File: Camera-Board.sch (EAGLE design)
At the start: 87 parts, among them J1 RJ45KEYSTONE-942, J10 BNC, J11 BNC, J12 BNC, J13 BNC, J14 BNC, J2 JTAG_ARM_10PIN, J3 APP_2POS_CONFIG12V_HORIZ, J4 BNC, J5 BNC, J6 BNC, J7 BNC, J9 BNC, U1 TM4C1294NCPDT, U2 HX1198FNL, U3 SLVU2.8-4, U4 OKI-78SR-5/1.5-W36HC, U5 TPS73733DCQ, U6 MAX4312ESE, U8 MAX4312ESE, Y1 NX3225GA, Y2 CRYATL_32K_SMD

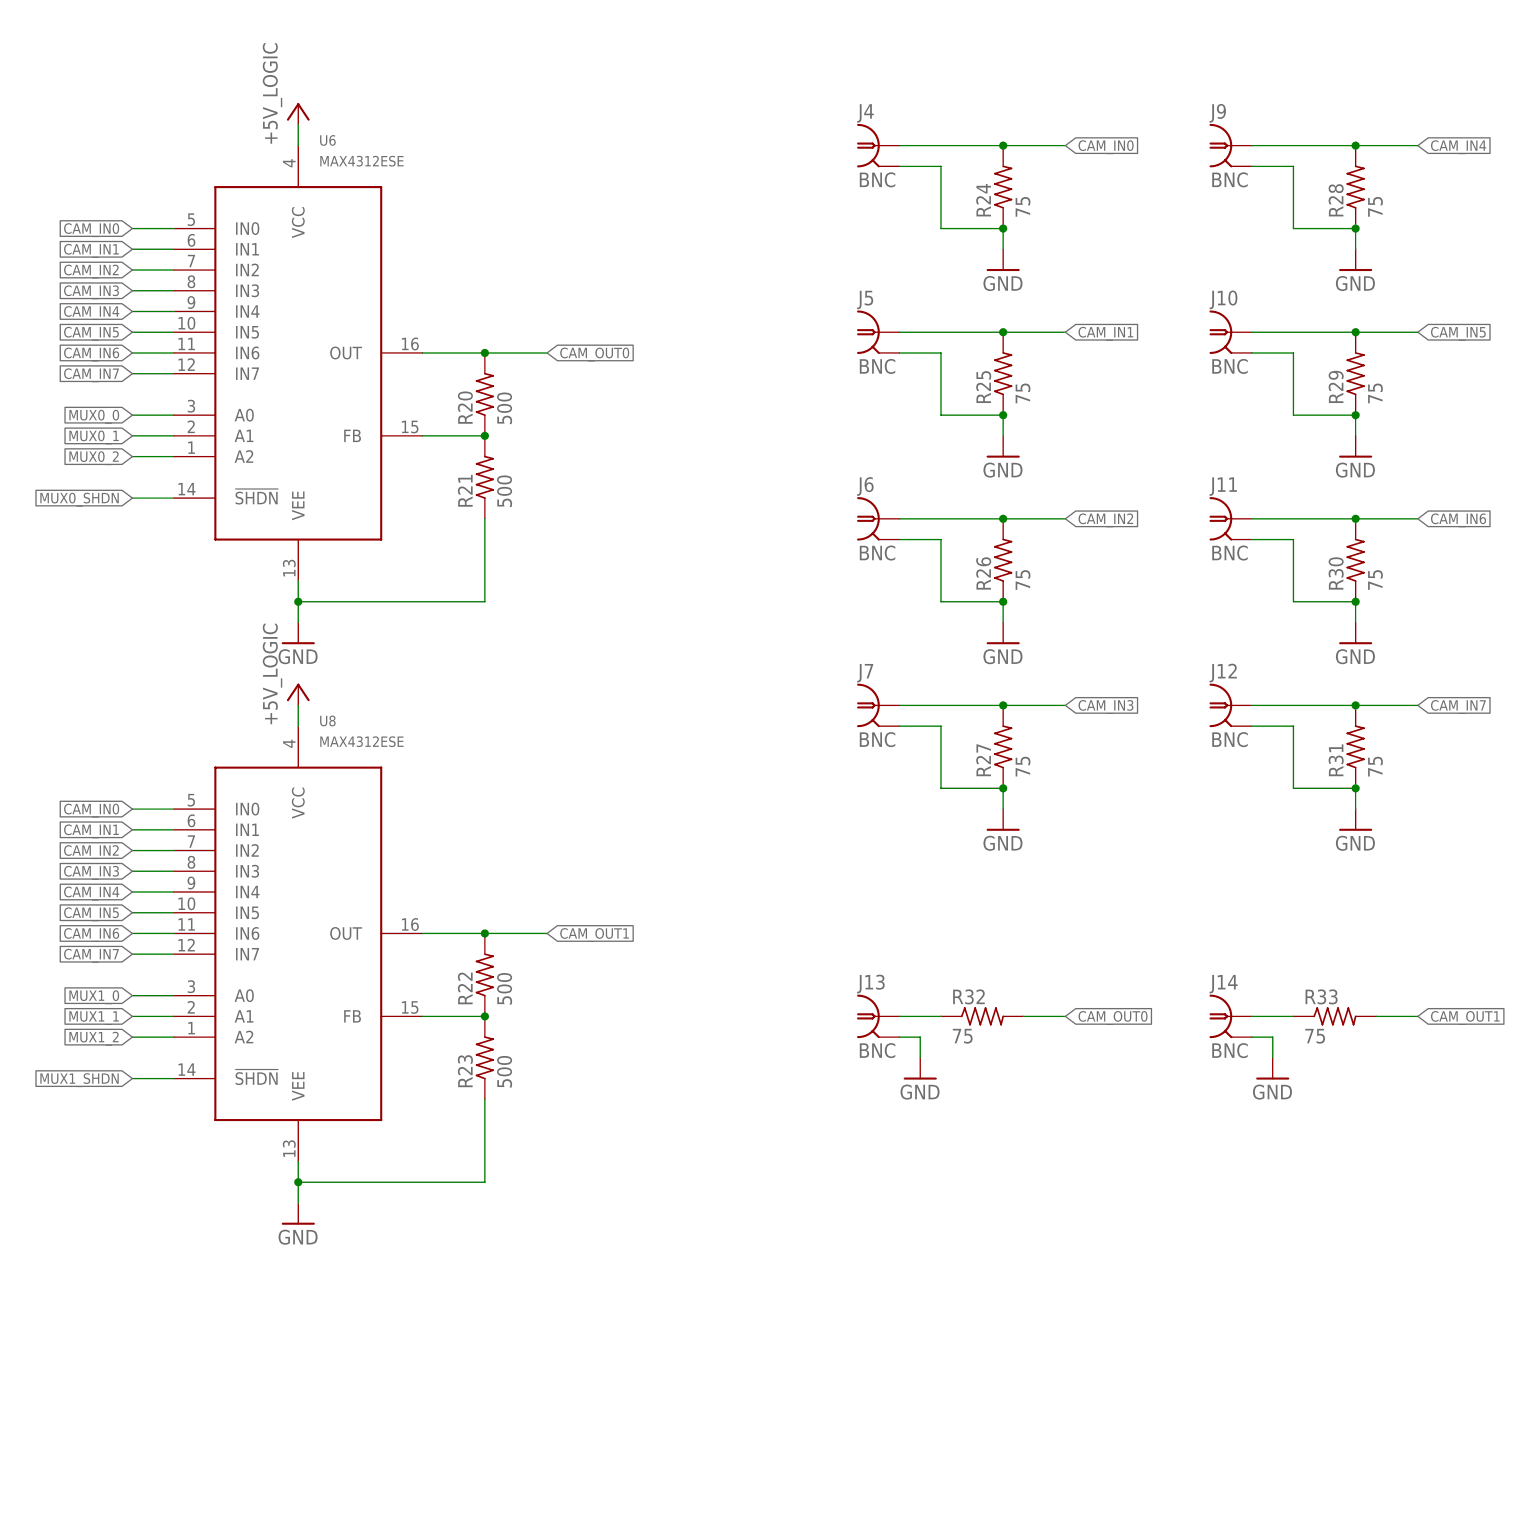
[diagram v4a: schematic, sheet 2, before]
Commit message: Final touches
Made board larger
Added more space between BNCs
Added more mounting holes
Updated Slik text and added signature
Arranged component labels
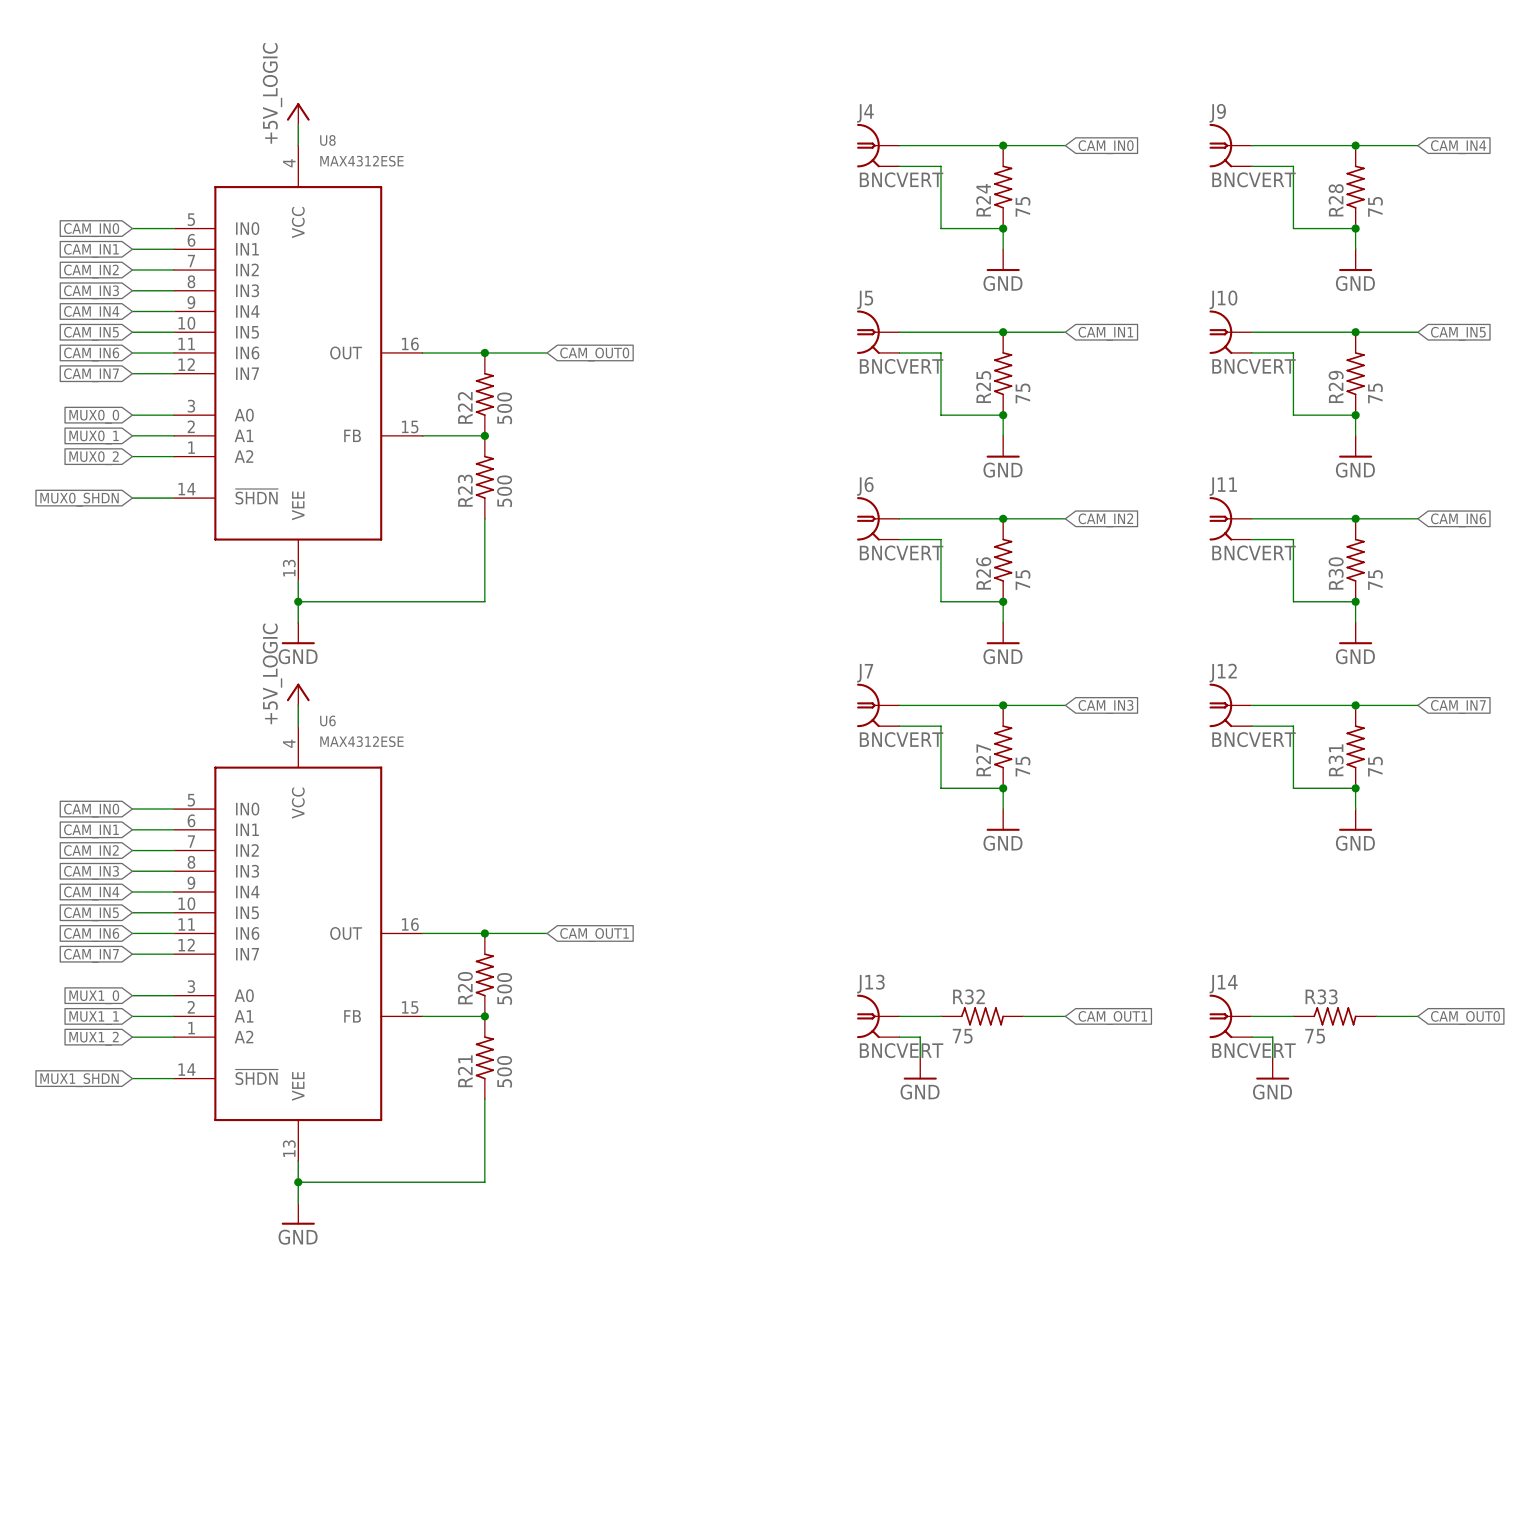
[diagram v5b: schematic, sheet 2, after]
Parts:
- added U$8: SIG3, sig:SIG3
- J10, J11, J12, J13, J14, J4, J5, J6, J7, J9: value BNC -> BNCVERT; device MRDT-Connectors:BNC -> MRDT-Connectors:BNCVERT
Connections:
- net CAM_OUT0: now also R22.2, R33.2, U8.OUT; no longer R20.2, R32.2, U6.OUT
- net CAM_OUT1: now also R20.2, R32.2, U6.OUT; no longer R22.2, R33.2, U8.OUT
- net MUX0_0: now also U1G$1.PD0@1, U8.A0; no longer U1G$1.PD7@128, U6.A0
- net MUX0_1: now also U1G$1.PD1@2, U8.A1; no longer U1G$1.PD6@127, U6.A1
- net MUX0_2: now also U1G$1.PD2@3, U8.A2; no longer U1G$1.PD5@126, U6.A2
- net MUX0_SHDN: now also U1G$1.PD3@4, U8.!SHDN; no longer U1G$1.PD4@125, U6.!SHDN
- net MUX1_0: now also U1G$1.PD7@128, U6.A0; no longer U1G$1.PD0@1, U8.A0
- net MUX1_1: now also U1G$1.PD6@127, U6.A1; no longer U1G$1.PD1@2, U8.A1
- net MUX1_2: now also U1G$1.PD5@126, U6.A2; no longer U1G$1.PD2@3, U8.A2
- net MUX1_SHDN: now also U1G$1.PD4@125, U6.!SHDN; no longer U1G$1.PD3@4, U8.!SHDN
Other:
- moved on the sheet: R20, R21, R22, R23, U6, U8
